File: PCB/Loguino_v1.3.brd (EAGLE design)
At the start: 89.9 x 66 mm, 47 parts, among them X1 22-23-2041, X4 22-23-2041, X5 22-23-2021

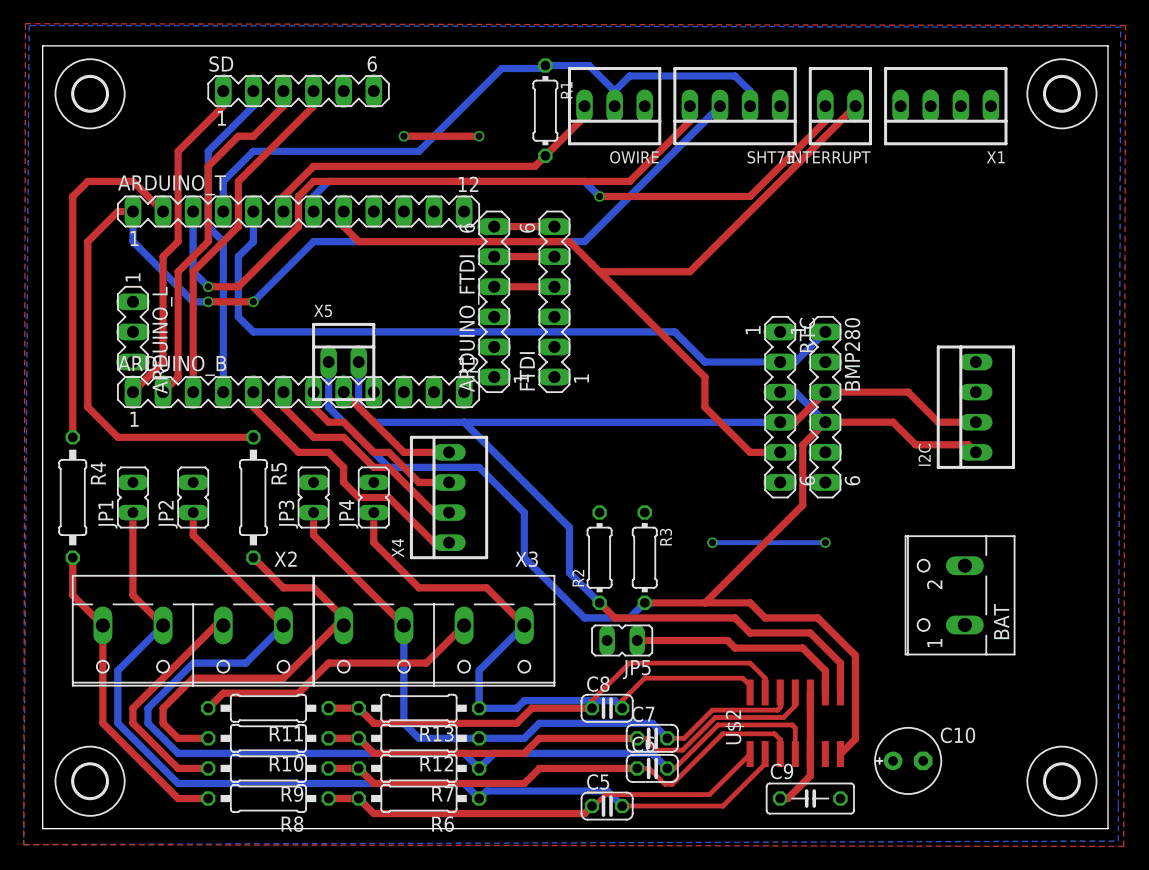
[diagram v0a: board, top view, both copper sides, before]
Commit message: updated PCB and sketches to v1.3
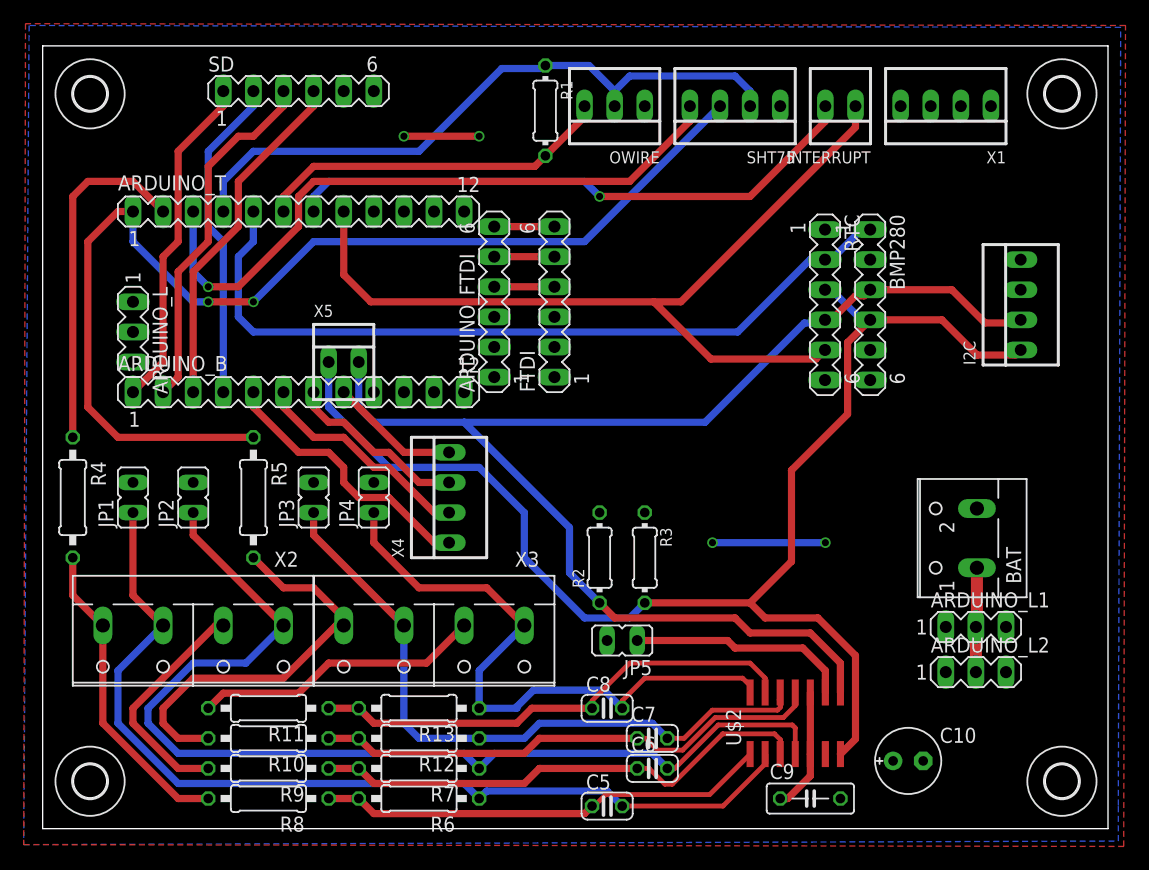
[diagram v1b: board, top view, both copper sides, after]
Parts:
- added ARDUINO_L1, ARDUINO_L2: (no value), con-lstb:MA03-1
- moved RTC 9.43 mm to (66.0, 44.2)
- moved I2C 9.43 mm to (82.5, 44.2)
- moved BMP280 9.43 mm to (69.8, 44.2)
- moved BAT 4.93 mm to (77.6, 24.5)
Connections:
- new net N$1: ARDUINO_L1.2, ARDUINO_L2.2, BAT.1
- net VCC: now also ARDUINO_L1.1, ARDUINO_L2.1; no longer BAT.1
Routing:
- net SDA: track 107.1 -> 116.9 mm
- net N$1: track 0.00 -> 8.84 mm
- net SCL: track 103.4 -> 111.0 mm
- net EN_RTC: track 61.6 -> 66.9 mm
- net N$23: track 52.3 -> 53.2 mm
- net INT0: track 74.9 -> 74.1 mm
